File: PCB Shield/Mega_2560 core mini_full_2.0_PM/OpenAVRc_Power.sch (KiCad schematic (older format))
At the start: 16 parts, among them P17 BATT, P21 Sw_power, P26 LCD_Alim, P30 MiniDCDC3A, U4 L4941, U5 LD1117S33TR

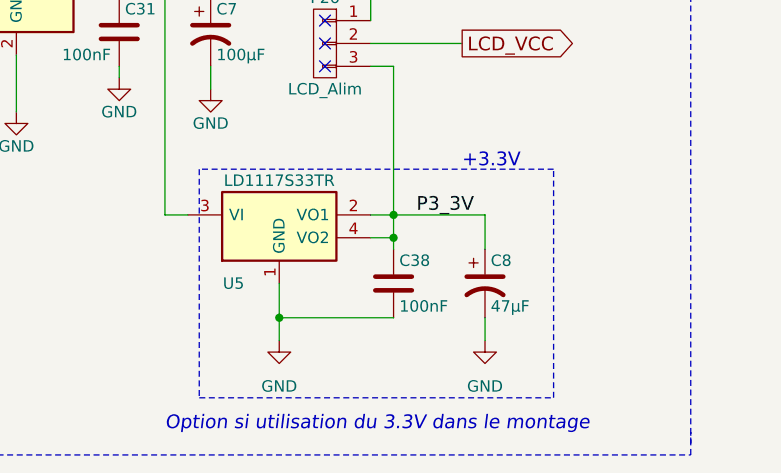
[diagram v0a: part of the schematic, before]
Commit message: Replace P3_3V signal by +3,3V (solve no connected plane on top)
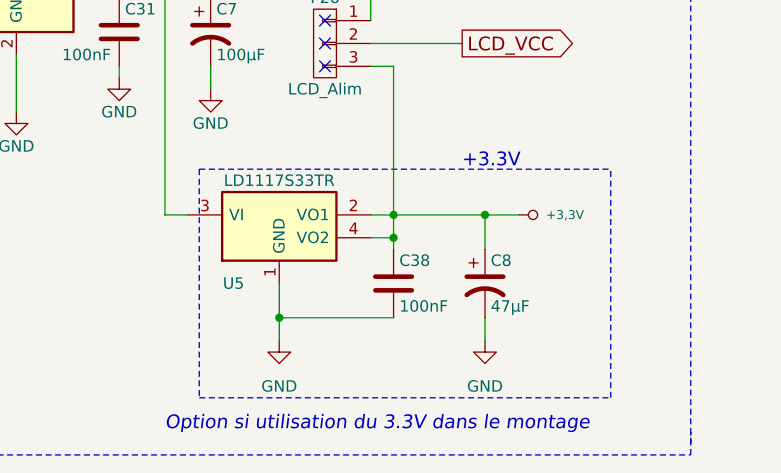
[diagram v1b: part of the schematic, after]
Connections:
- net P3_3V renamed +3.3V
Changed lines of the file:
@@
 $EndComp
 $Comp
-L GND-RESCUE-Mega_2560_core_mini_full_2.0 #PWR0108
+L GND-RESCUE-Mega_2560_core_mini_full_2.0 #PWR0110
 U 1 1 59C5313F
 P 7550 4550
-F 0 "#PWR0108" H 7550 4300 50  0001 C CNN
+F 0 "#PWR0110" H 7550 4300 50  0001 C CNN
 F 1 "GND" H 7550 4350 50  0000 C CNN
 F 2 "" H 7550 4550 50  0000 C CNN
@@
 +5V
 $Comp
-L VCC #PWR0109
+L VCC #PWR0111
 U 1 1 59C5314F
 P 8200 3000
-F 0 "#PWR0109" H 8200 2850 50  0001 C CNN
+F 0 "#PWR0111" H 8200 2850 50  0001 C CNN
 F 1 "VCC" V 8200 3200 50  0000 C CNN
 F 2 "" H 8200 3000 50  0000 C CNN
@@
 Power Management
 $Comp
-L GND-RESCUE-Mega_2560_core_mini_full_2.0 #PWR0110
+L GND-RESCUE-Mega_2560_core_mini_full_2.0 #PWR0112
 U 1 1 59C5315D
 P 6400 3550
-F 0 "#PWR0110" H 6400 3300 50  0001 C CNN
+F 0 "#PWR0112" H 6400 3300 50  0001 C CNN
 F 1 "GND" H 6400 3400 50  0000 C CNN
 F 2 "" H 6400 3550 50  0000 C CNN
@@
 $EndComp
 $Comp
-L GND-RESCUE-Mega_2560_core_mini_full_2.0 #PWR0111
+L GND-RESCUE-Mega_2560_core_mini_full_2.0 #PWR0113
 U 1 1 59C53163
 P 5250 4350
-F 0 "#PWR0111" H 5250 4100 50  0001 C CNN
+F 0 "#PWR0113" H 5250 4100 50  0001 C CNN
 F 1 "GND" H 5250 4200 50  0000 C CNN
 F 2 "" H 5250 4350 50  0000 C CNN
@@
 $EndComp
 $Comp
-L GND-RESCUE-Mega_2560_core_mini_full_2.0 #PWR0112
+L GND-RESCUE-Mega_2560_core_mini_full_2.0 #PWR0114
 U 1 1 59C53189
 P 6850 3400
-F 0 "#PWR0112" H 6850 3150 50  0001 C CNN
+F 0 "#PWR0114" H 6850 3150 50  0001 C CNN
 F 1 "GND" H 6850 3250 50  0000 C CNN
 F 2 "" H 6850 3400 50  0000 C CNN
@@
 $EndComp
 $Comp
-L GND-RESCUE-Mega_2560_core_mini_full_2.0 #PWR0113
+L GND-RESCUE-Mega_2560_core_mini_full_2.0 #PWR0115
 U 1 1 59C53196
 P 5900 3400
-F 0 "#PWR0113" H 5900 3150 50  0001 C CNN
+F 0 "#PWR0115" H 5900 3150 50  0001 C CNN
 F 1 "GND" H 5900 3250 50  0000 C CNN
 F 2 "" H 5900 3400 50  0000 C CNN
@@
 $EndComp
 $Comp
-L GND-RESCUE-Mega_2560_core_mini_full_2.0 #PWR0114
+L GND-RESCUE-Mega_2560_core_mini_full_2.0 #PWR0116
 U 1 1 59C531AC
 P 7250 3450
-F 0 "#PWR0114" H 7250 3200 50  0001 C CNN
+F 0 "#PWR0116" H 7250 3200 50  0001 C CNN
 F 1 "GND" H 7250 3300 50  0000 C CNN
 F 2 "" H 7250 3450 50  0000 C CNN
@@
 $EndComp
 $Comp
-L GND-RESCUE-Mega_2560_core_mini_full_2.0 #PWR0115
+L GND-RESCUE-Mega_2560_core_mini_full_2.0 #PWR0117
 U 1 1 59C531B9
 P 8450 4550
-F 0 "#PWR0115" H 8450 4300 50  0001 C CNN
+F 0 "#PWR0117" H 8450 4300 50  0001 C CNN
 F 1 "GND" H 8450 4350 50  0000 C CNN
 F 2 "" H 8450 4550 50  0000 C CNN
@@
 Text Notes 4450 2700 0    60   ~ 0
 Power Switch
-Text Label 8150 4000 0    60   ~ 0
-P3_3V
 $Comp
 L CONN_01X08 P30
@@
 $EndComp
 $Comp
-L GND-RESCUE-Mega_2560_core_mini_full_2.0 #PWR0116
+L GND-RESCUE-Mega_2560_core_mini_full_2.0 #PWR0118
 U 1 1 59C531C8
 P 3600 4550
-F 0 "#PWR0116" H 3600 4300 50  0001 C CNN
+F 0 "#PWR0118" H 3600 4300 50  0001 C CNN
 F 1 "GND" H 3600 4400 50  0000 C CNN
 F 2 "" H 3600 4550 50  0000 C CNN
@@
 $EndComp
 $Comp
-L VCC #PWR0117
+L VCC #PWR0119
 U 1 1 59C531CE
 P 3800 3900
-F 0 "#PWR0117" H 3800 3750 50  0001 C CNN
+F 0 "#PWR0119" H 3800 3750 50  0001 C CNN
 F 1 "VCC" H 3800 4000 50  0000 C CNN
 F 2 "" H 3800 3900 50  0000 C CNN
@@
 $EndComp
 $Comp
-L GND-RESCUE-Mega_2560_core_mini_full_2.0 #PWR0118
+L GND-RESCUE-Mega_2560_core_mini_full_2.0 #PWR0120
 U 1 1 59C531DF
 P 4100 3200
-F 0 "#PWR0118" H 4100 2950 50  0001 C CNN
+F 0 "#PWR0120" H 4100 2950 50  0001 C CNN
 F 1 "GND" H 4100 3050 50  0000 C CNN
 F 2 "" H 4100 3200 50  0000 C CNN
@@
 $EndComp
 $Comp
-L GND-RESCUE-Mega_2560_core_mini_full_2.0 #PWR0119
+L GND-RESCUE-Mega_2560_core_mini_full_2.0 #PWR0121
 U 1 1 59C531F4
 P 5600 4450
-F 0 "#PWR0119" H 5600 4200 50  0001 C CNN
+F 0 "#PWR0121" H 5600 4200 50  0001 C CNN
 F 1 "GND" H 5600 4300 50  0000 C CNN
 F 2 "" H 5600 4450 50  0000 C CNN
@@
 $EndComp
 $Comp
-L VCC #PWR0120
+L VCC #PWR0122
 U 1 1 59C531FA
 P 5600 3400
-F 0 "#PWR0120" H 5600 3250 50  0001 C CNN
+F 0 "#PWR0122" H 5600 3250 50  0001 C CNN
 F 1 "VCC" H 5600 3550 50  0000 C CNN
 F 2 "" H 5600 3400 50  0000 C CNN
@@
 $EndComp
 $Comp
-L +BATT #PWR0121
+L +BATT #PWR0123
 U 1 1 59C53200
 P 5250 2800
-F 0 "#PWR0121" H 5250 2650 50  0001 C CNN
+F 0 "#PWR0123" H 5250 2650 50  0001 C CNN
 F 1 "+BATT" H 5250 2940 50  0000 C CNN
 F 2 "" H 5250 2800 50  0000 C CNN
@@
 	1    0    0    -1
 $EndComp
-Text GLabel 8350 3250 2    60   Output ~ 0
-LCD_VCC
 Text Label 5900 2550 3    60   ~ 0
 DCDC_IN+
@@
 	7550 4450 8050 4450
 Wire Notes Line
-	8750 3800 7200 3800
+	7200 3800 9000 3800
 Wire Wire Line
 	6800 3000 8200 3000
 Wire Notes Line
-	8750 4800 8750 3800
-Wire Notes Line
-	7200 4800 8750 4800
+	7200 4800 9000 4800
 Wire Notes Line
 	7200 3800 7200 4800
@@
 	8450 4000 8450 4150
 Wire Wire Line
-	7950 4000 8450 4000
+	7950 4000 8600 4000
 Wire Wire Line
 	8450 4550 8450 4450
@@
 Text GLabel 5050 3900 0    60   Output ~ 0
 U_batt
+Connection ~ 8450 4000
+Wire Notes Line
+	9000 4800 9000 3800
+Text GLabel 8350 3250 2    60   Output ~ 0
+LCD_VCC
+$Comp
+L +3,3V #PWR0124
+U 1 1 59CA5551
+P 8600 4000
+F 0 "#PWR0124" H 8600 3960 30  0001 C CNN
+F 1 "+3,3V" V 8600 4200 39  0000 C CNN
+F 2 "" H 8600 4000 60  0001 C CNN
+F 3 "" H 8600 4000 60  0001 C CNN
+	1    8600 4000
+	0    1    1    0
+$EndComp
 $EndSCHEMATC

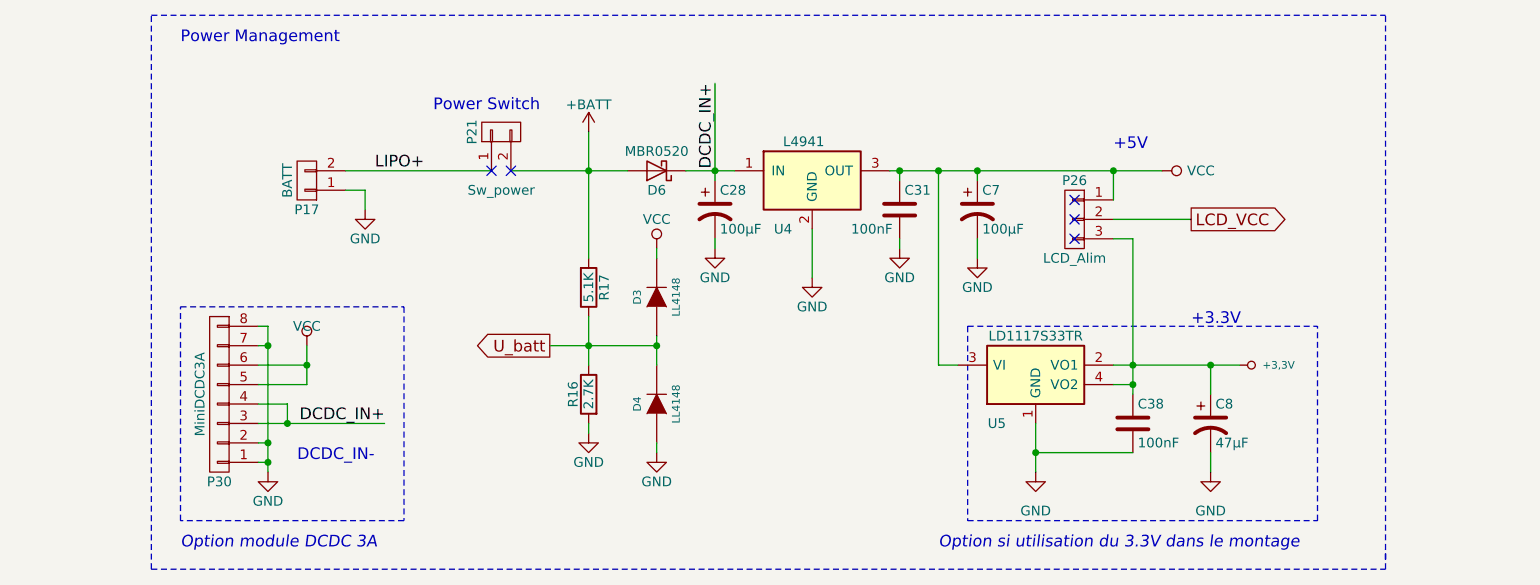
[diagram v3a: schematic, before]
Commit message: Update schematic and pcb
Add PM-5033 as other dc/dc option
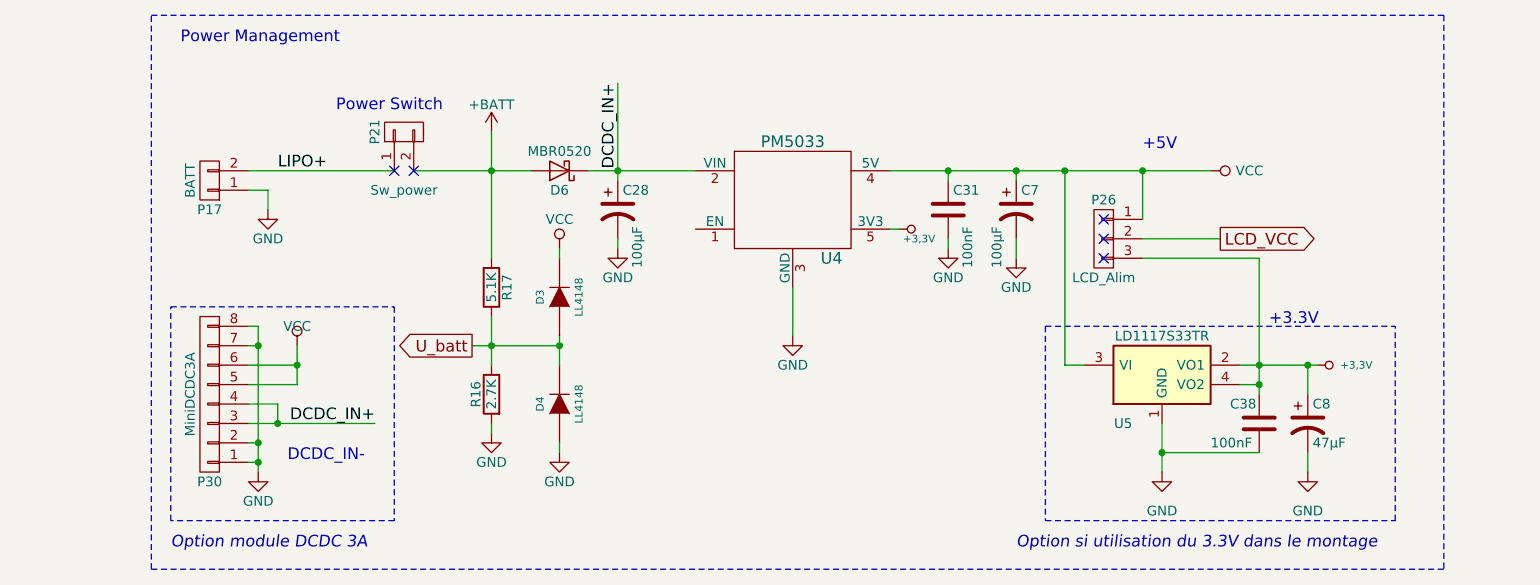
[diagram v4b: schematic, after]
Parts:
- removed U4: L4941, Power_Integrations:TO-220, symbol L4941
- added U4: PM5033, PM5033_SIL5, symbol PM5033
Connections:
- net +3.3V: now also U4.5 (3V3)
- net DCDC_IN+: now also U4.2 (VIN)
- net GND: now also U4.3 (GND)
- net VCC: now also U4.4 (5V)
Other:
- moved on the sheet: C28, C31, C38, C7, C8, D3, D4, D6, P17, P21, P26, P30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

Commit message: Add Hold Power feature
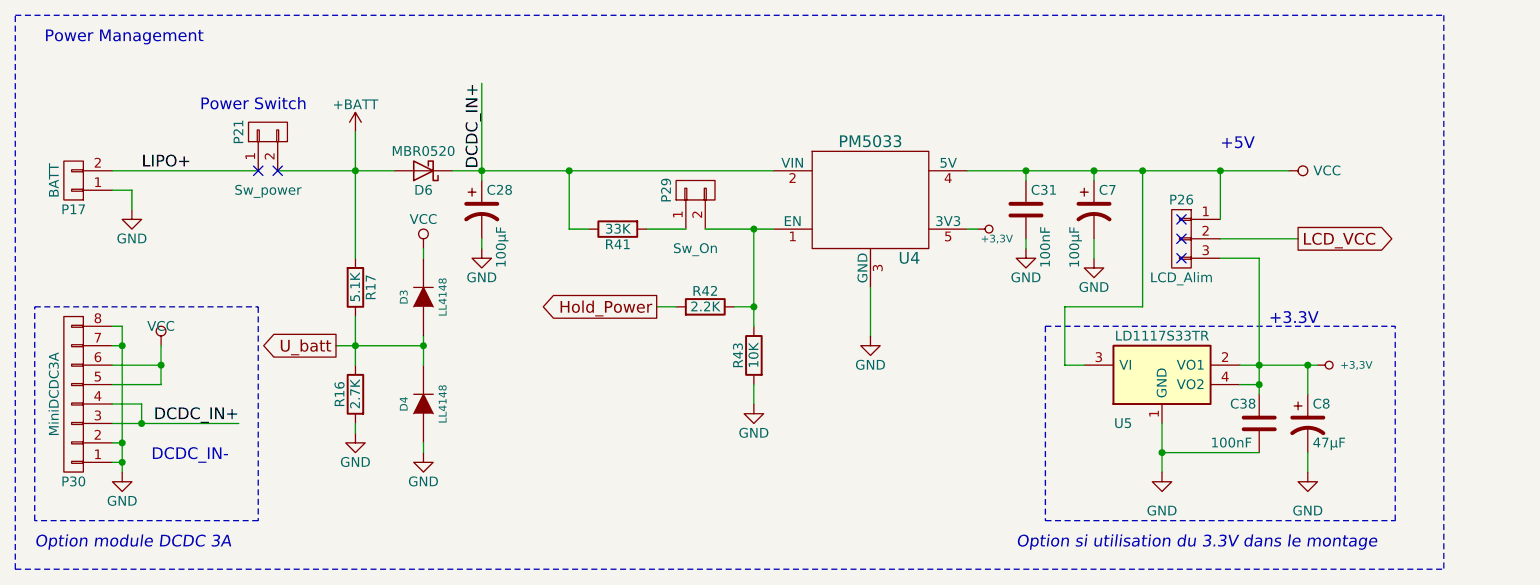
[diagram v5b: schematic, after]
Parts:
- added P29: Sw_On, Pin_Headers:Pin_Header_Straight_1x02_Pitch2.54mm, symbol CONN_01X02
- added R41: 33K, Resistors_SMD:R_1206, symbol R-RESCUE-Mega_2560_core_mini_full_2.0
- added R42: 2.2K, Resistors_SMD:R_1206, symbol R-RESCUE-Mega_2560_core_mini_full_2.0
- added R43: 10K, Resistors_SMD:R_1206, symbol R-RESCUE-Mega_2560_core_mini_full_2.0
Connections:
- net DCDC_IN+: now also R41.1
- net GND: now also R43.2
- net at U4.1 (EN): now also P29.2 (P2), R42.1, R43.1
- new net: P29.1 (P1), R41.2
- new net Hold_Power: R42.2
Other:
- moved on the sheet: C28, C31, C7, D3, D4, D6, P17, P21, P26, P30, R16, R17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

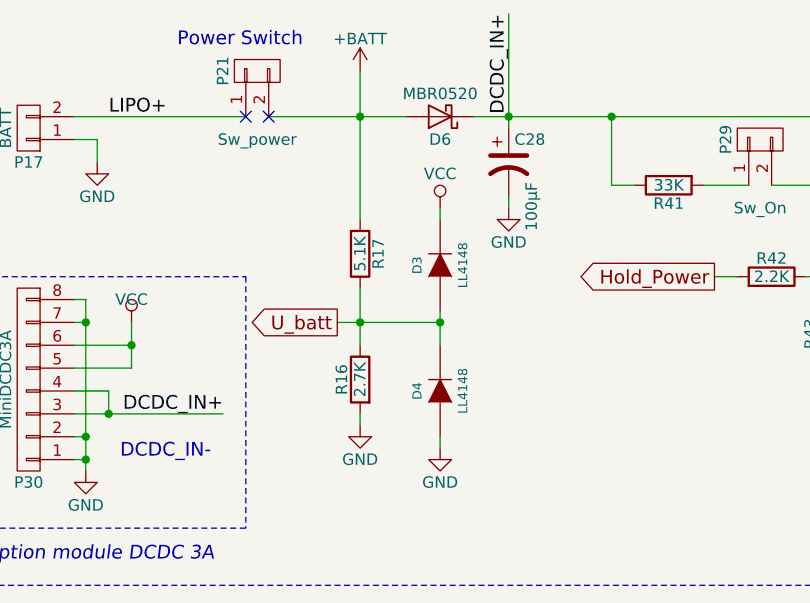
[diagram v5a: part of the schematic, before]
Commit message: Update shield files before new fabrication
delete two diodes on Vbatt .
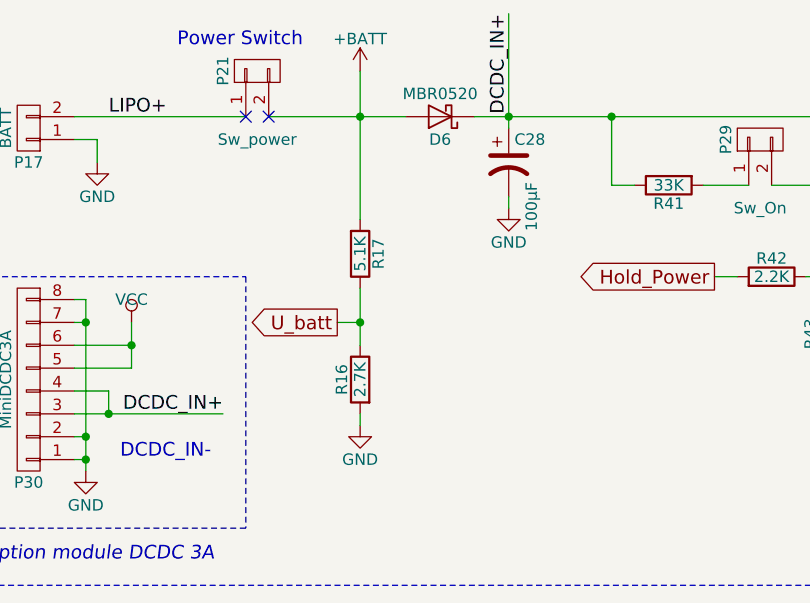
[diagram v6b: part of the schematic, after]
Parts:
- removed D3, D4: LL4148, D_SCD80_HandSoldering, symbol DIODE
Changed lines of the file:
@@
 Option module DCDC 3A
-$Comp
-L DIODE D3
-U 1 1 59C531E6
-P 4400 3650
-F 0 "D3" H 4400 3750 40  0000 C CNN
-F 1 "LL4148" H 4400 3550 40  0000 C CNN
-F 2 "D_SCD80_HandSoldering" H 4400 3650 60  0001 C CNN
-F 3 "" H 4400 3650 60  0000 C CNN
-	1    4400 3650
-	0    -1   -1   0
-$EndComp
-$Comp
-L DIODE D4
-U 1 1 59C531ED
-P 4400 4200
-F 0 "D4" H 4400 4300 40  0000 C CNN
-F 1 "LL4148" H 4400 4100 40  0000 C CNN
-F 2 "D_SCD80_HandSoldering" H 4400 4200 60  0001 C CNN
-F 3 "" H 4400 4200 60  0000 C CNN
-	1    4400 4200
-	0    -1   -1   0
-$EndComp
-$Comp
-L GND-RESCUE-Mega_2560_core_mini_full_2.0 #PWR0124
-U 1 1 59C531F4
-P 4400 4450
-F 0 "#PWR0124" H 4400 4200 50  0001 C CNN
-F 1 "GND" H 4400 4300 50  0000 C CNN
-F 2 "" H 4400 4450 50  0000 C CNN
-F 3 "" H 4400 4450 50  0000 C CNN
-	1    4400 4450
-	1    0    0    -1
-$EndComp
-$Comp
-L VCC #PWR0125
-U 1 1 59C531FA
-P 4400 3400
-F 0 "#PWR0125" H 4400 3250 50  0001 C CNN
-F 1 "VCC" H 4400 3550 50  0000 C CNN
-F 2 "" H 4400 3400 50  0000 C CNN
-F 3 "" H 4400 3400 50  0000 C CNN
-	1    4400 3400
-	1    0    0    -1
-$EndComp
 $Comp
 L +BATT #PWR0126
@@
 Wire Notes Line
 	2400 4800 2400 3700
-Wire Wire Line
-	4400 3850 4400 4000
-Wire Wire Line
-	4400 3400 4400 3450
-Wire Wire Line
-	3950 3900 4400 3900
-Connection ~ 4400 3900
-Wire Wire Line
-	4400 4450 4400 4400
 Wire Notes Line
 	2300 5050 2300 2200
@@
 Wire Wire Line
 	7700 3700 7700 4000
+Wire Wire Line
+	4050 3900 3950 3900
 $EndSCHEMATC
